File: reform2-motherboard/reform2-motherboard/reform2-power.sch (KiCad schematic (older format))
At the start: 171 parts, among them J1 Jack-DC, J12 BATCON1, J13 BATCON2, J8 USB_B_Micro, Q1 Si4850BDY, Q10 PMV50EPEAR, Q11 PMV50EPEAR, Q12 PMV50EPEAR, Q13 PMV55ENEA, Q2 Si4850BDY, Q3 PMV55ENEA, Q4 PMV55ENEA, Q5 PMV50EPEAR, Q6 PMV50EPEAR, Q7 PMV50EPEAR, Q8 PMV50EPEAR, Q9 PMV50EPEAR, SW1 SW_Push, SW2 SW_Push, U12 LM2677-3.3, U13 TLV71312PDBV, U14 TLV71311PDBV, U17 TLV1117-18, U18 LPC11U24FBD48-301, U19 TLV1117-15, U2 LTC4162-F, U3 LTC4359-MS8, U4 LTC6803-4, U5 LTC4359-MS8, U6 INA260, U7 LM2596T-5, U8 LM2596T-ADJ, Y2 12MHz

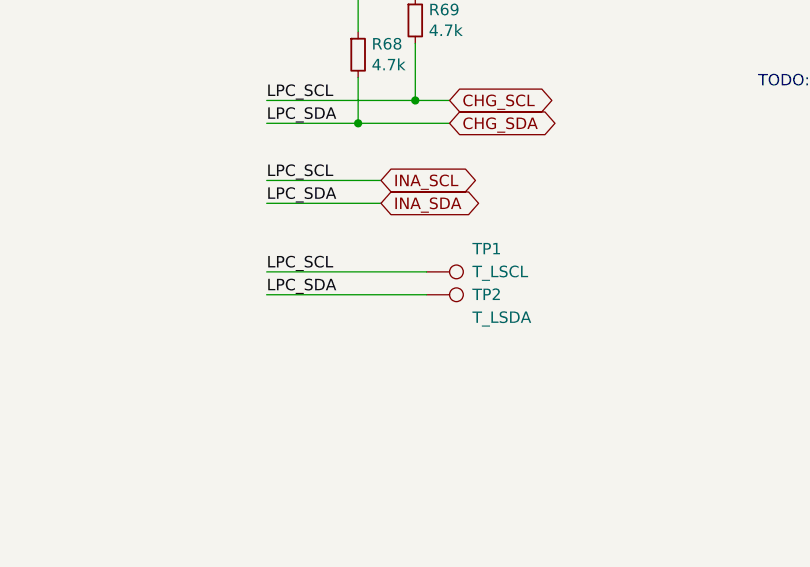
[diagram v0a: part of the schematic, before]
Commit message: WIP: reform2 motherboard: bulk of signal routing done
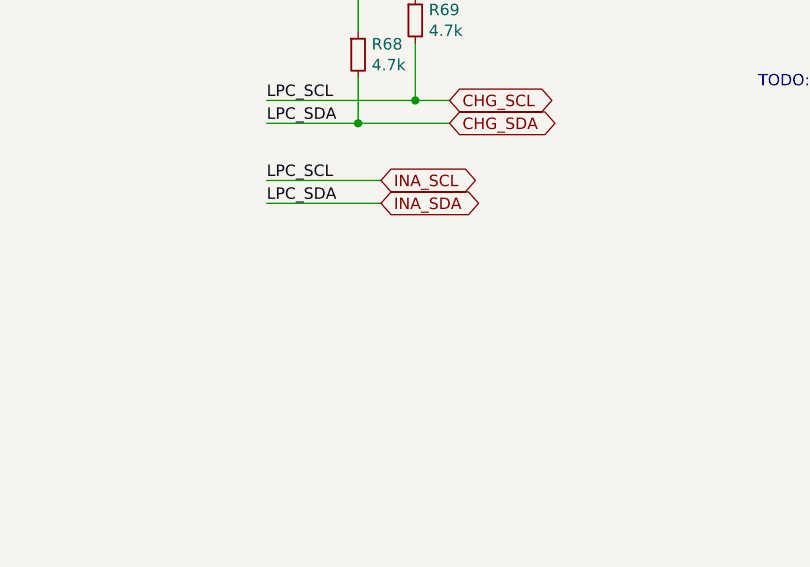
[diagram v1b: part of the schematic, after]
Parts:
- removed TP1: T_LSCL, TestPoint:TestPoint_Pad_1.0x1.0mm, symbol Connector:TestPoint
- removed TP2: T_LSDA, TestPoint:TestPoint_Pad_1.0x1.0mm, symbol Connector:TestPoint
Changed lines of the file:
@@
 Wire Wire Line
 	2750 9150 2250 9150
-Text Label 2250 9550 0    50   ~ 0
-LPC_SDA
-Text Label 2250 9450 0    50   ~ 0
-LPC_SCL
-$Comp
-L Connector:TestPoint TP1
-U 1 1 608E9805
-P 2950 9450
-F 0 "TP1" V 2850 9650 50  0000 L CNN
-F 1 "T_LSCL" V 2950 9650 50  0000 L CNN
-F 2 "TestPoint:TestPoint_Pad_1.0x1.0mm" H 3150 9450 50  0001 C CNN
-F 3 "~" H 3150 9450 50  0001 C CNN
-	1    2950 9450
-	0    1    1    0
-$EndComp
-Wire Wire Line
-	2250 9450 2950 9450
-$Comp
-L Connector:TestPoint TP2
-U 1 1 60939E8A
-P 2950 9550
-F 0 "TP2" V 2950 9750 50  0000 L CNN
-F 1 "T_LSDA" V 3050 9750 50  0000 L CNN
-F 2 "TestPoint:TestPoint_Pad_1.0x1.0mm" H 3150 9550 50  0001 C CNN
-F 3 "~" H 3150 9550 50  0001 C CNN
-	1    2950 9550
-	0    1    1    0
-$EndComp
-Wire Wire Line
-	2250 9550 2950 9550
 $Comp
 L Device:R_Small R69

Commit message: reform2: first motherboard fully routed, checks TBD
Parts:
- added J22: LPC_IO, Connector_PinHeader_2.54mm:PinHeader_2x08_P2.54mm_Vertical, symbol Connector_Generic:Conn_02x08_Odd_Even
- added R157: 0, Resistor_SMD:R_0603_1608Metric, symbol Device:R_Small
- R123: value 2.4k 1% -> 3k 1%
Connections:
- net +3V3: now also J22.15 (Pin_15)
- net GND: now also J22.16 (Pin_16)
- net LPC_AD5: now also J22.2 (Pin_2)
- net LPC_AD7: now also J22.13 (Pin_13)
- net LPC_MISO1a: now also J22.8 (Pin_8)
- net LPC_RXDc: now also J22.4 (Pin_4)
- net LPC_SCK0b: now also J22.10 (Pin_10)
- net LPC_SSEL0: now also R157.1
- net LPC_SWDIO: now also J22.1 (Pin_1)
- net LPC_TDI: now also J22.9 (Pin_9)
- net LPC_TDO: now also J22.5 (Pin_5)
- net LPC_TMS: now also J22.7 (Pin_7)
- net LPC_TRST: now also J22.3 (Pin_3)
- net LPC_TXDc: now also J22.6 (Pin_6)
- net LPC_UVBUS: now also J22.11 (Pin_11)
- net LPC_PIO1_25: now reaches U18.1 (PIO1_25)
- net LPC_PIO1_25: now also J22.14 (Pin_14)
- net LPC_PIO1_31: now reaches U18.25 (PIO1_31)
- net LPC_PIO1_31: now also J22.12 (Pin_12)
- net LPC_PIO1_16: now reaches U18.48 (PIO1_16)
- net LPC_RXDb renamed LPC_UART2_RX
- net LPC_TXDb renamed LPC_UART2_TX
- new net LPC_SS0: R157.2
- no-connect marks 9 -> 21
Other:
- note added: "MAYBE: isolate serial"
- note added: "MAYBE: isolate?"
- note added: "actually 5V"
- note added: "pins 3 and 7 are NC"
- note removed: "TODO: connect LPC/IMX serial"
- note removed: "TODO: isolate serial"
- note removed: "TODO: isolate?"
- note removed: "TODO: where is pin 3 and 7???"
- note removed: "Up to 3A @ 4.2V"
- moved on the sheet: R128, R73, R74, R75, R76, SW1, SW2

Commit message: reform2 motherboard: pinout and footprint checks completed; ERC checks fixed 100%
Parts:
- added C31: 0.1uF, symbol Device:C_Small
- added J23: POWERS, Connector_PinHeader_2.54mm:PinHeader_1x04_P2.54mm_Vertical, symbol Connector:Conn_01x04_Male
- added TP3: T_CHGALERT, TestPoint:TestPoint_Pad_D1.0mm, symbol Connector:TestPoint
- U7: symbol Regulator_Switching:LM2596T-5 -> lm2596t:LM2596T-5
- U8: symbol Regulator_Switching:LM2596T-ADJ -> lm2596t:LM2596T-ADJ
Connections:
- net +3V3: now also U2.15 (DVCC), J23.3 (Pin_3)
- net GND: now also U7.6 (GND), U8.6 (GND), C31.1, J23.4 (Pin_4); no longer U2.12 (SMBALERT), U2.15 (DVCC), U7.5 (~ON~/OFF), U8.5 (~ON~/OFF)
- net at C34.1, Q2.5 (D), Q2.6 (D)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: now also C31.2
- net LPC_NCTS renamed LPC_~CTS
- net LPC_NDTR renamed LPC_~DTR
- net LPC_NRESET renamed LPC_~RESET
- net LPC_NUSBCON renamed LPC_~USBCON
- net LPC_SCLKb renamed LPC_PIO1_24
- net LPC_TRST renamed LPC_~TRST
- new net: TP3.1, U2.12 (SMBALERT)
- new net ~ON~_SOM: J23.2 (Pin_2), U8.5 (~ON~/OFF)
- new net ~ON~_USB: J23.1 (Pin_1), U7.5 (~ON~/OFF)
- no-connect marks 21 -> 20
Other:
- note added: "MAX 100V"
- note added: "PROBLEM: MAX 35V VIN. USE 32V INPUT?"
- moved on the sheet: C16, C56, J1, R54

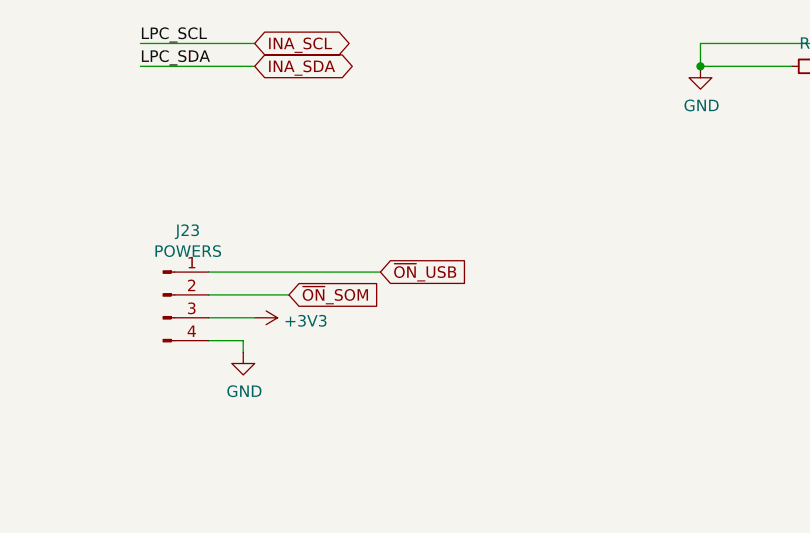
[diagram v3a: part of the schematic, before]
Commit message: reform2 motherboard: PCB DRC 100%
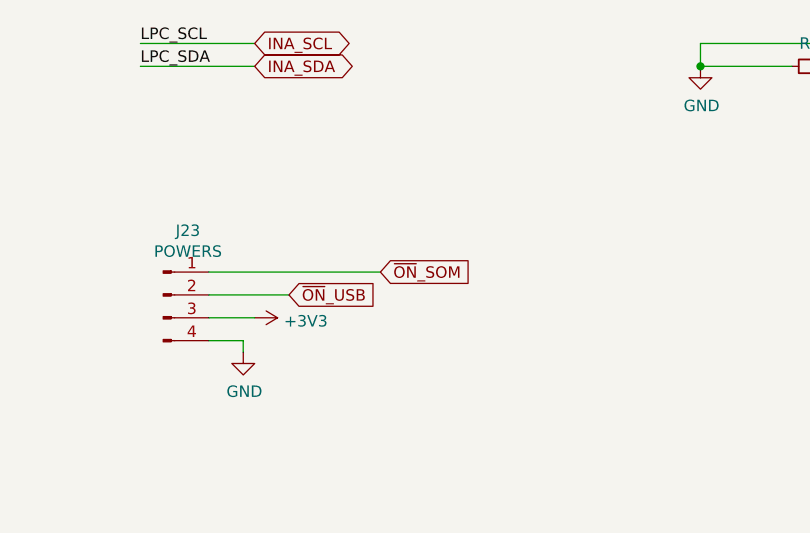
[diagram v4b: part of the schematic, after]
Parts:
- C31: footprint (none) -> Capacitor_SMD:C_0603_1608Metric
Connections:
- net ~ON~_SOM: now also J23.1 (Pin_1); no longer J23.2 (Pin_2)
- net ~ON~_USB: now also J23.2 (Pin_2); no longer J23.1 (Pin_1)
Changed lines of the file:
@@
 	1    0    0    -1
 $EndComp
+Text GLabel 2900 10150 2    50   Input ~ 0
+~ON~_USB
 Text GLabel 3300 10050 2    50   Input ~ 0
-~ON~_USB
-Text GLabel 2900 10150 2    50   Input ~ 0
 ~ON~_SOM
 Wire Wire Line
@@
 F 0 "C31" V 4171 3200 50  0000 C CNN
 F 1 "0.1uF" V 4262 3200 50  0000 C CNN
-F 2 "" H 4400 3200 50  0001 C CNN
+F 2 "Capacitor_SMD:C_0603_1608Metric" H 4400 3200 50  0001 C CNN
 F 3 "~" H 4400 3200 50  0001 C CNN
 	1    4400 3200

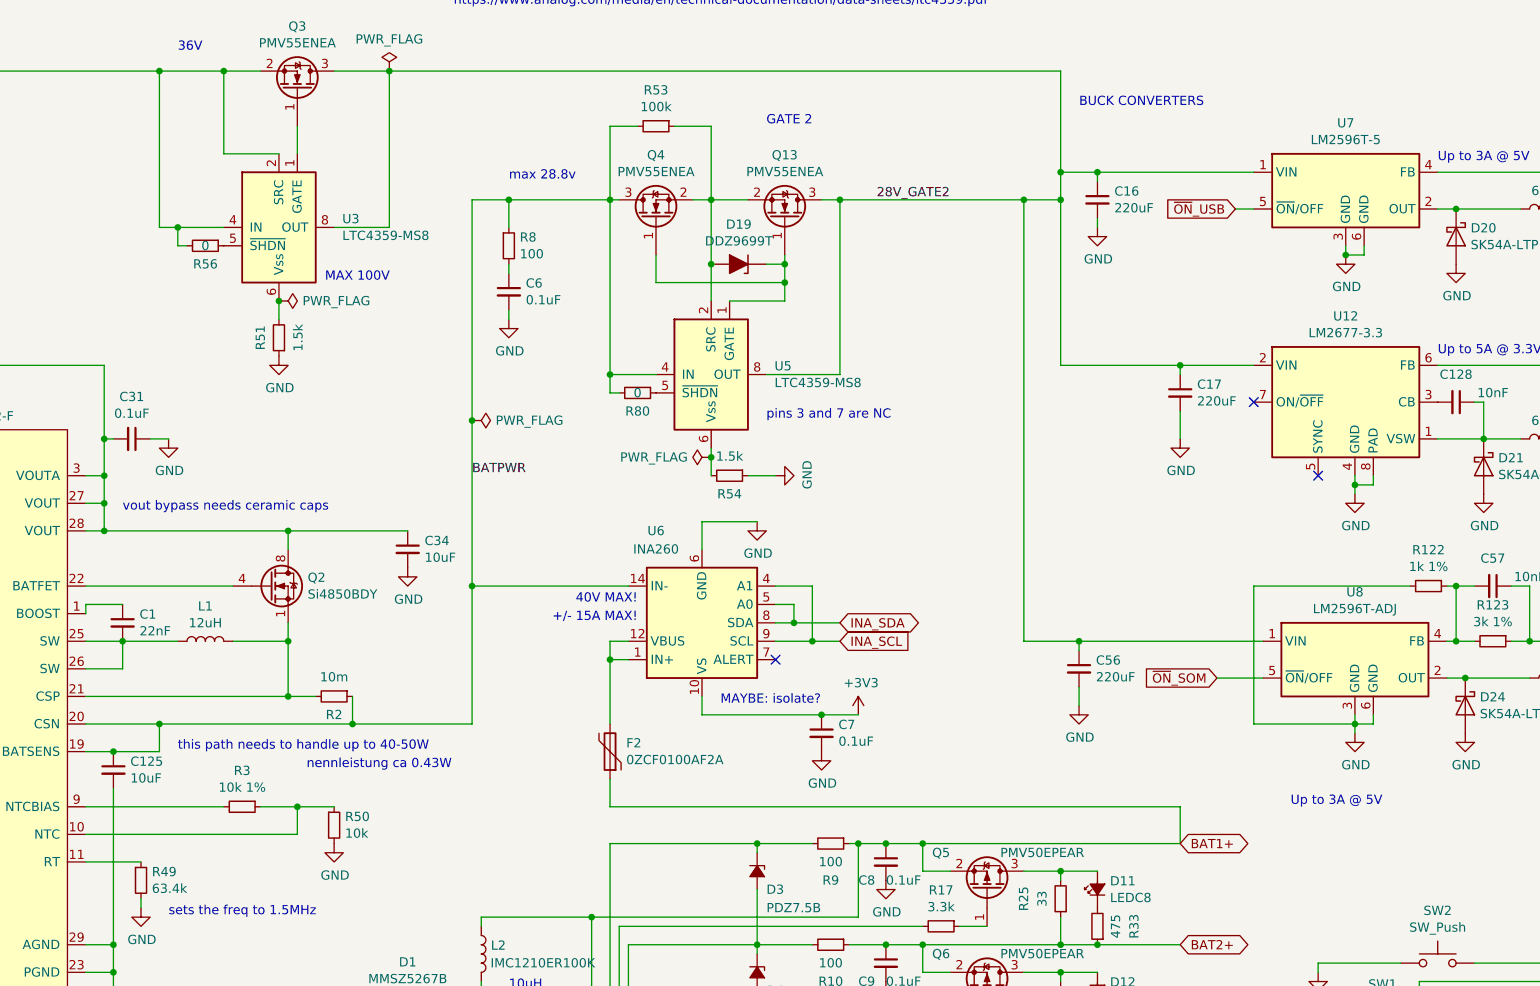
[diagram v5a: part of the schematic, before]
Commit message: reform2 motherboard: add part numbers
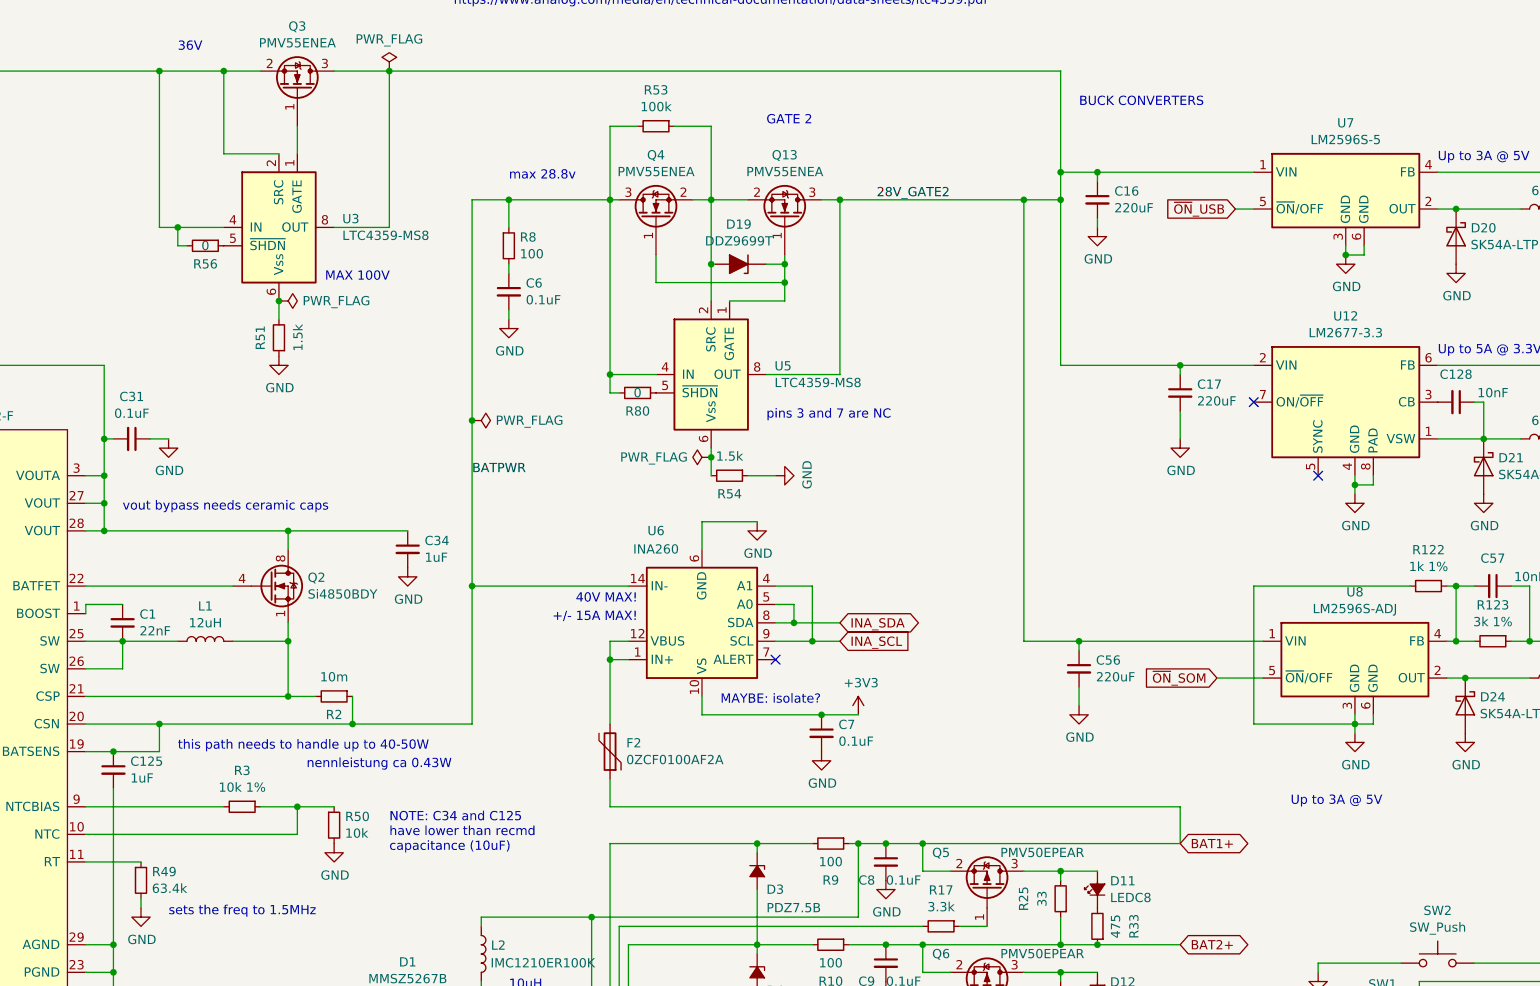
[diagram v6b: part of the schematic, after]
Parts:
- C10, C11, C12, C13, C14, C15, C49, C50, C6, C7, C8, C9: Manufacturer TDK -> Yageo; Manufacturer_No CGA3E2X8R1E104K080AE -> CC0603JPX7R9BB104
- C125, C34: value 10uF -> 1uF; Manufacturer_No LMK107BBJ106KALT -> UMK107BJ105KA-T
- C129, C130, C2, C32, C35, C36, C4, C5, C64, C65: Manufacturer_No JMK107C6105KA -> UMK107BJ105KA-T
- C16, C18, C19, C3, C62: Manufacturer Panasonic -> KEMET; Manufacturer_No EEE-FT1H221GP -> EDH226M050S9GAA
- C31: Manufacturer (none) -> Yageo; Manufacturer_No (none) -> CC0603JPX7R9BB104
- C37, C38, C46, C47: Manufacturer Taiyo Yuden -> TDK; Manufacturer_No LMK107BBJ106KALT -> CGA3E2X8R1E104K080AE
- J22: Manufacturer (none) -> Molex; Manufacturer_No (none) -> 87914-1616
- J23: Manufacturer (none) -> Wurth; Manufacturer_No (none) -> 61300411121
- R122: Manufacturer (none) -> Vishay Dale; Manufacturer_No (none) -> CRCW06031K00FKEAC
- R123: Manufacturer (none) -> Yageo; Manufacturer_No (none) -> RC0603FR-073KL
- R53: Manufacturer Susumu -> Vishay Dale; Manufacturer_No RR0816P-104-D -> CRCW0603100KJNEAC
- U7: value LM2596T-5 -> LM2596S-5
- U8: value LM2596T-ADJ -> LM2596S-ADJ; Manufacturer (none) -> Texas Instruments; Manufacturer_No (none) -> LM2596T-ADJ
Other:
- note added: "NOTE: C34 and C125\nhave lower than recmd\ncapacitance (10uF)"

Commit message: Reform 2 Rev 2 WIP: fixed various Rev 1 bugs; consolidate battery connector; consolidate 5v powers; make power rails switchable by LPC; exchange TUSB QFN for TQFP; remove eDP FPC; fixes holes; add SD level shifter; add PCIe clock generator; reduce JTAG footprint
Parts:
- removed C56, C62: 220uF, Capacitor_SMD:CP_Elec_8x10, symbol Device:C_Small
- removed C57: 10nF, Capacitor_SMD:C_0603_1608Metric, symbol Device:C_Small
- removed D13: LEDC6, LED_SMD:LED_0603_1608Metric, symbol Device:LED_Small_ALT
- removed D14: LEDC5, LED_SMD:LED_0603_1608Metric, symbol Device:LED_Small_ALT
- removed D15: LEDC4, LED_SMD:LED_0603_1608Metric, symbol Device:LED_Small_ALT
- removed D16: LEDC3, LED_SMD:LED_0603_1608Metric, symbol Device:LED_Small_ALT
- removed D17, D18: LEDC2, LED_SMD:LED_0603_1608Metric, symbol Device:LED_Small_ALT
- removed D24: SK54A-LTP, Diode_SMD:D_SMA, symbol Diode:1N5821
- removed J12: BATCON1, Connector_Molex:Molex_Micro-Fit_3.0_43650-0500_1x05_P3.00mm_Horizontal, symbol Connector:Conn_01x05_Male
- removed J13: BATCON2, Connector_Molex:Molex_Micro-Fit_3.0_43650-0500_1x05_P3.00mm_Horizontal, symbol Connector:Conn_01x05_Male
- removed L5: 68uH, Inductor_SMD:L_Bourns_SRR1210A, symbol Device:L
- removed R122: 1k 1%, Resistor_SMD:R_0603_1608Metric, symbol Device:R_Small
- removed R123: 3k 1%, Resistor_SMD:R_0603_1608Metric, symbol Device:R_Small
- removed R34, R35, R36, R37, R38, R39, R40: 475, Resistor_SMD:R_0603_1608Metric, symbol Device:R_Small
- removed SW1: SW_Push, Button_Switch_SMD:SW_Push_1P1T_NO_CK_KMR2, symbol Switch:SW_Push
- removed U7: LM2596S-5, Package_TO_SOT_SMD:TO-263-5_TabPin6, symbol lm2596t:LM2596T-5
- removed U8: LM2596S-ADJ, Package_TO_SOT_SMD:TO-263-5_TabPin6, symbol lm2596t:LM2596T-ADJ
- added C148: 10nF, Capacitor_SMD:C_0603_1608Metric, symbol Device:C_Small
- added J2: BATCON, footprints:Molex-1054051110, symbol Connector:Conn_01x11_Male
- added Q14, Q15: PMV50EPEAR, Package_TO_SOT_SMD:SOT-23, symbol Transistor_FET:DMG2301L
- added R163, R165: 0, Resistor_SMD:R_0603_1608Metric, symbol Device:R_Small
- added R164: 475, Resistor_SMD:R_0603_1608Metric, symbol Device:R_Small
- added SW1: SW_DIP_x01, Button_Switch_SMD:SW_DIP_SPSTx01_Slide_Omron_A6S-110x_W8.9mm_P2.54mm, symbol Switch:SW_DIP_x01
- added U7: LM2677SX-5, Package_TO_SOT_SMD:TO-263-7_TabPin8, symbol reform2:LM2677-3.3
- C2: value 1uF -> 0.1uF; Manufacturer Taiyo Yuden -> (none); Manufacturer_No UMK107BJ105KA-T -> (none)
- D10, D3, D4, D5, D6, D7, D8, D9: value PDZ7.5B -> PDZ7.5BGWJ; footprint Diode_SMD:D_SOD-323 -> Diode_SMD:D_SOD-123
- D11: value LEDC8 -> LED3V
- D12: value LEDC7 -> LED5V
- R128: value 0 -> 10k
- U12: value LM2677-3.3 -> LM2677SX-3.3
- Y2: symbol reform2-motherboard-rescue:Crystal_Small-reform-motherboard-rescue -> Device:Crystal_GND24_Small
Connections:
- net ~ON~_SOM is gone; now on net ON_SOM: J23.1 (Pin_1)
- net ~ON~_USB is gone; now on net +5V: J23.2 (Pin_2)
- net +3V3: now also D11.2 (A), Q15.3 (D); no longer C46.1, C47.1, C49.1, C50.1, L4.2, U12.6 (FB), U18.44 (VDD), U18.8 (VDD)
- net +5V: now also D12.2 (A), U7.6 (FB)
- net 28V_GATE2: now also U12.7 (ON/~OFF~), Q14.2 (S), U7.2 (VIN)
- net BAT1+: now also J2.1 (Pin_1)
- net BAT2+: now also J2.2 (Pin_2); no longer R33.1
- net BAT3+: now also J2.3 (Pin_3)
- net BAT4+: now also J2.4 (Pin_4)
- net BAT5+: now also J2.6 (Pin_6)
- net BAT6+: now also J2.7 (Pin_7)
- net BAT7+: now also J2.8 (Pin_8)
- net BAT8+: now also J2.9 (Pin_9)
- net BMON_SDI: now also R75.1; no longer R74.1
- net BMON_SDO: now also R74.1; no longer R75.1
- net GND: now also R33.1, Y2.2, Y2.4, J2.10 (Pin_10), J2.11 (Pin_11), J2.5 (Pin_5), R164.1, SW1.1, U7.4 (GND), U7.8 (PAD)
- net LPC_UFTOGG: now also SW1.2
- net at Q5.3 (D), R25.2: no longer D11.2 (A)
- net at Q6.3 (D), R26.2: no longer D12.2 (A)
- net at D12.1 (K): now also R164.2
- net at D20.1 (K), L3.1: now also C148.1, U7.1 (VSW)
- net at C51.1, U18.6 (XTALIN): now also Y2.3; no longer Y2.2
- net +36V: no longer names the net of F1.2, J1.1
- net 36V_IN renamed 32V_IN
- net LPC_PIO1_16 renamed EN_3V3
- net EN_3V3: now also R165.1
- net LPC_PIO1_24 renamed IMX_WAKE
- net LPC_SCK1a renamed EN_5V
- net EN_5V: now also R163.1
- net LPC_~DTR renamed ON_SOM
- new net: C46.1, C47.1, C49.1, C50.1, L4.2, Q15.2 (S), U12.6 (FB), U18.44 (VDD), U18.8 (VDD)
- new net: Q15.1 (G), R165.2
- new net: Q14.1 (G), R163.2
- new net: Q14.3 (D), U7.7 (ON/~OFF~)
- new net: C148.2, U7.3 (CB)
- no-connect marks 20 -> 16
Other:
- note added: "32V"
- note added: "32VDC"
- note added: "Molex NanoFit"
- note added: "Replace with general 3v3 switch"
- note added: "TODO: LED array or I2C screen on keyboard for system status"
- note added: "TODO: add power cycle DIP"
- note added: "TODO: keyboard cable with UART to LPC?"
- note added: "TODO:\n1. physical switch for 3v3\n2. 8x LED moved to LPC control? how to identify problematic cells?\n3. 5v switch is controlled by LPC, can be bypassed by DIP switch\n4. LPC checks cell health when powered, alerts of problems\n"
- note added: "Up to 5A @ 5V"
- note removed: "36V"
- note removed: "36VDC"
- note removed: "MAYBE: isolate serial"
- note removed: "MAYBE: isolate?"
- note removed: "Molex MicroFit 3.0"
- note removed: "PROBLEM: MAX 35V VIN. USE 32V INPUT?"
- note removed: "Up to 3A @ 5V"
- note removed: "actually 5V"
- moved on the sheet: C128, C130, C17, C18, C19, D11, D20, D21, L3, L4, R124, R125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
